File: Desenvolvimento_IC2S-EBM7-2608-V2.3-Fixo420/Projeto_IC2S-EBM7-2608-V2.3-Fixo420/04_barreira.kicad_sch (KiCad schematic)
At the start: 9 parts, among them T3 TP_DGND, T5 TP_+3.3V_DIG, U2 SPX3819M5-L-3-3/TR, U5 ISO7141CCDBQR

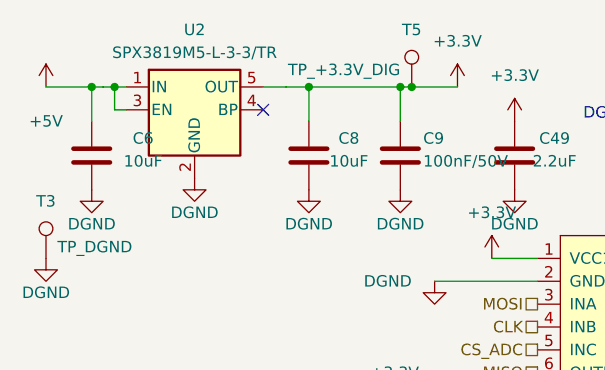
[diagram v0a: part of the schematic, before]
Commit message: Roteamento do U2 (SPX3819) e do bypass do ISO7141; pacote de fabricacao regenerado
PCB:
- C49 (2,2 uF) e C8 (10 uF) junto do VOUT do U2 (1,68 e 2,23 mm), C6 na
  entrada a 3,0 mm.
- C9 (100 nF) reposto como bypass do VCC1 do U5 (1,93 mm), massa por via
  DGND a 1,0 mm do pad. Tinha sido movido com o grupo do U2 (6,3 mm).
- Rede unconnected-(U2-BP-Pad4) na classe DIGSIDE (pad NC do SPX3819 dentro
  da zona DGND; sem isto a regra de barreira de 1,0 mm disparava contra C9).
- DRC kicad-cli com paridade: 0 erros, 0 avisos, 0 desligados, paridade 0.

Esquematico: sem alteracao electrica (paridade 0, netlist igual). Restauro do
historico local do KiCad: coordenadas arredondadas (02), fios colineares
fundidos com os mesmos extremos (04), rectangulo grafico removido (06),
ordem dos textos (08).

Fabricacao: Gerbers, furacao, PnP, stencil, BOM, vistas, STEP e PDF do
esquematico regenerados desta placa (antes eram de 28-09 02:48).

Co-Authored-By: Claude Opus 5.5 (1M context) <noreply@anthropic.com>
Claude-Session: https://claude.ai/code/session_01KPnkiJQKrkjgRqqw9M78ie
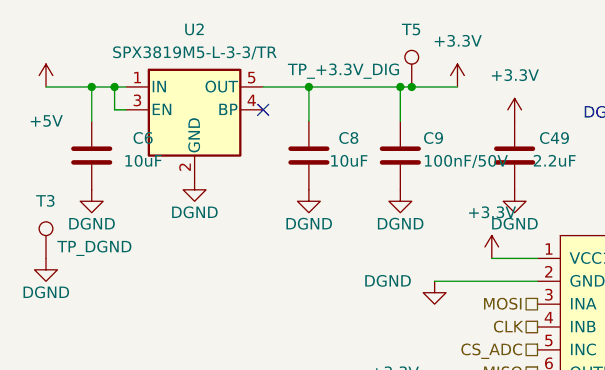
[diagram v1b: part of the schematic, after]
